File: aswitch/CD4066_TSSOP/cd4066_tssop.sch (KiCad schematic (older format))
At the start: 17 parts, among them P1 CONN_01X02, P10 CONN_01X01, P11 CONN_01X01, P12 CONN_01X01, P13 CONN_01X01, P14 CONN_01X01, P2 CONN_01X02, P3 CONN_01X01, P4 CONN_01X01, P5 CONN_01X01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

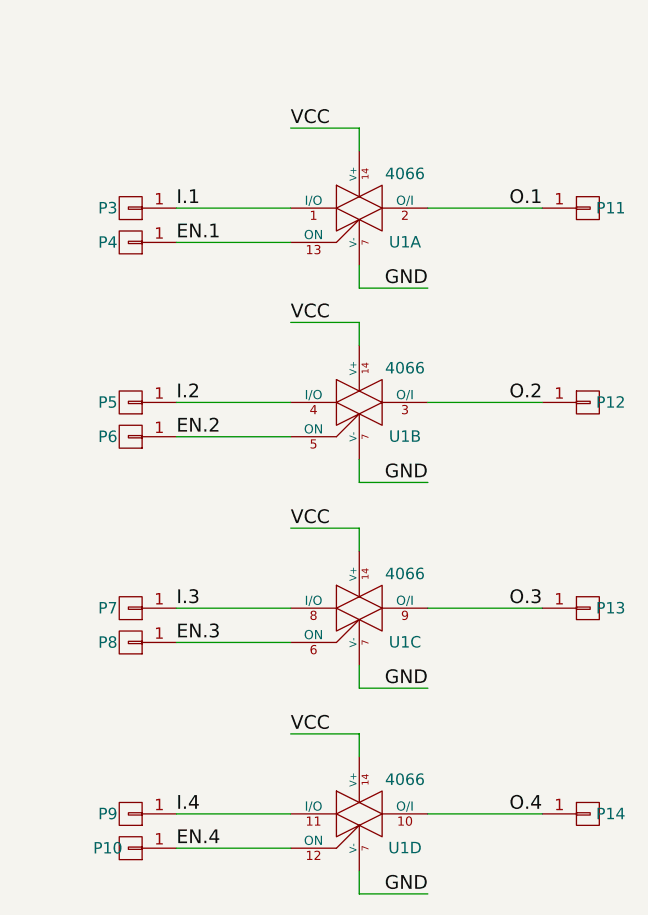
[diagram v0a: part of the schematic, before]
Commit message: Re-export gerbers at 0.1mm default line width, update .schs with KiField, wget wavegen ICL 8083
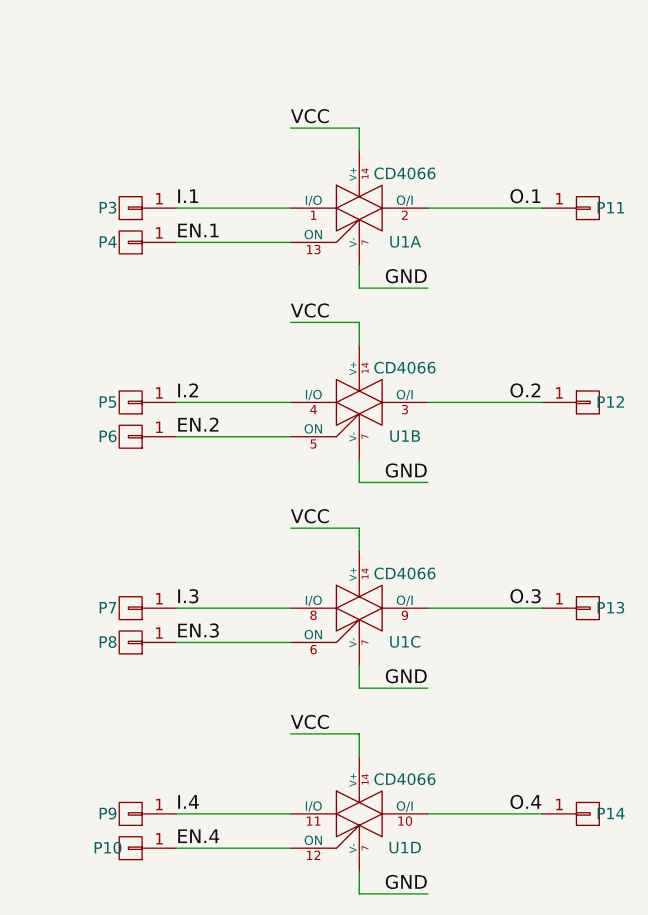
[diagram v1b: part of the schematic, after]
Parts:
- U1: value 4066 -> CD4066; Dist [1] Part # (none) -> 595-CD4066BPWR; Dist [1] Source (none) -> http://www2.mouser.com/ProductDetail/Texas-Instruments/CD40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; Mfr (none) -> Texas Instruments; Mfr Part # (none) -> CD4066BPWR
